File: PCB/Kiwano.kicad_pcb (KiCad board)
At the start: 2 copper layers, 63 x 63 mm, 50 parts, among them J1 VIK Module, J2 Cirque, J3 RGB_EX, SW1 PER56, U1 PMW3360DM-T2QU, U2 AP2127K-ADJ

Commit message: Fixed silk, moved production files.
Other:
- board text removed: "MISO Pullup"
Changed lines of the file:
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@@
     (property "ki_keywords" "R resistor")
     (attr smd)
-    (fp_text reference "R6" (at 0 1.5 180) (layer "B.SilkS")
+    (fp_text reference "R6" (at 0.3 1.5 180) (layer "B.SilkS")
         (effects (font (size 1 1) (thickness 0.15)) (justify mirror))
     )
@@
     (property "ki_keywords" "R resistor")
     (attr smd)
-    (fp_text reference "R9" (at 0 1.399998 -180) (layer "B.SilkS")
+    (fp_text reference "R9" (at -0.3 1.399998 -180) (layer "B.SilkS")
         (effects (font (size 1 1) (thickness 0.15)) (justify mirror))
     )
@@
     )
   )
-  (gr_line (start 84.7 46.3) (end 84.3 45.899999)
-    (stroke (width 0.12) (type default)) (layer "B.SilkS"))
-  (gr_line (start 81.6 47.1) (end 81.6 46.3)
-    (stroke (width 0.12) (type default)) (layer "B.SilkS"))
-  (gr_line (start 82 45.9) (end 84.3 45.899999)
+  (gr_line (start 84.8 35.35) (end 85 35.55)
     (stroke (width 0.12) (type default)) (layer "B.SilkS"))
   (gr_line (start 64.400013 52.729992) (end 63.700007 52.729992)
     (stroke (width 0.12) (type default)) (layer "B.SilkS"))
-  (gr_line (start 83.5 35.8) (end 83.5 37.1)
+  (gr_line (start 83.8 35.05) (end 83.8 36.35)
     (stroke (width 0.12) (type default)) (layer "B.SilkS"))
   (gr_line (start 83.1 54.8) (end 83.1 54)
     (stroke (width 0.12) (type default)) (layer "B.SilkS"))
-  (gr_line (start 81.6 46.3) (end 82 45.9)
+  (gr_line (start 81.8 35.3) (end 81.8 35)
+    (stroke (width 0.12) (type default)) (layer "B.SilkS"))
+  (gr_line (start 81.8 35.3) (end 81.6 35.5)
     (stroke (width 0.12) (type default)) (layer "B.SilkS"))
   (gr_line (start 63.700009 55.700002) (end 63.700007 57.179993)
@@
   (gr_line (start 63.700003 52.729994) (end 63.699998 54.2)
     (stroke (width 0.12) (type default)) (layer "B.SilkS"))
-  (gr_line (start 84.6 35) (end 85 35.4)
+  (gr_line (start 84.8 35.35) (end 84.8 35.05)
     (stroke (width 0.12) (type default)) (layer "B.SilkS"))
-  (gr_line (start 84.5 35.8) (end 84.5 37.1)
+  (gr_line (start 82.8 35.05) (end 82.8 36.35)
     (stroke (width 0.12) (type default)) (layer "B.SilkS"))
   (gr_circle (center 75 60) (end 76.149999 58.008146)
@@
     (effects (font (size 1 1) (thickness 0.15)) (justify mirror))
   )
-  (gr_text "MISO\nPullup" (at 84.7 47.6) (layer "B.SilkS")
-    (effects (font (size 1 1) (thickness 0.15)) (justify right mirror))
-  )
   (gr_text "+5V" (at 62.899998 51.2) (layer "B.SilkS")

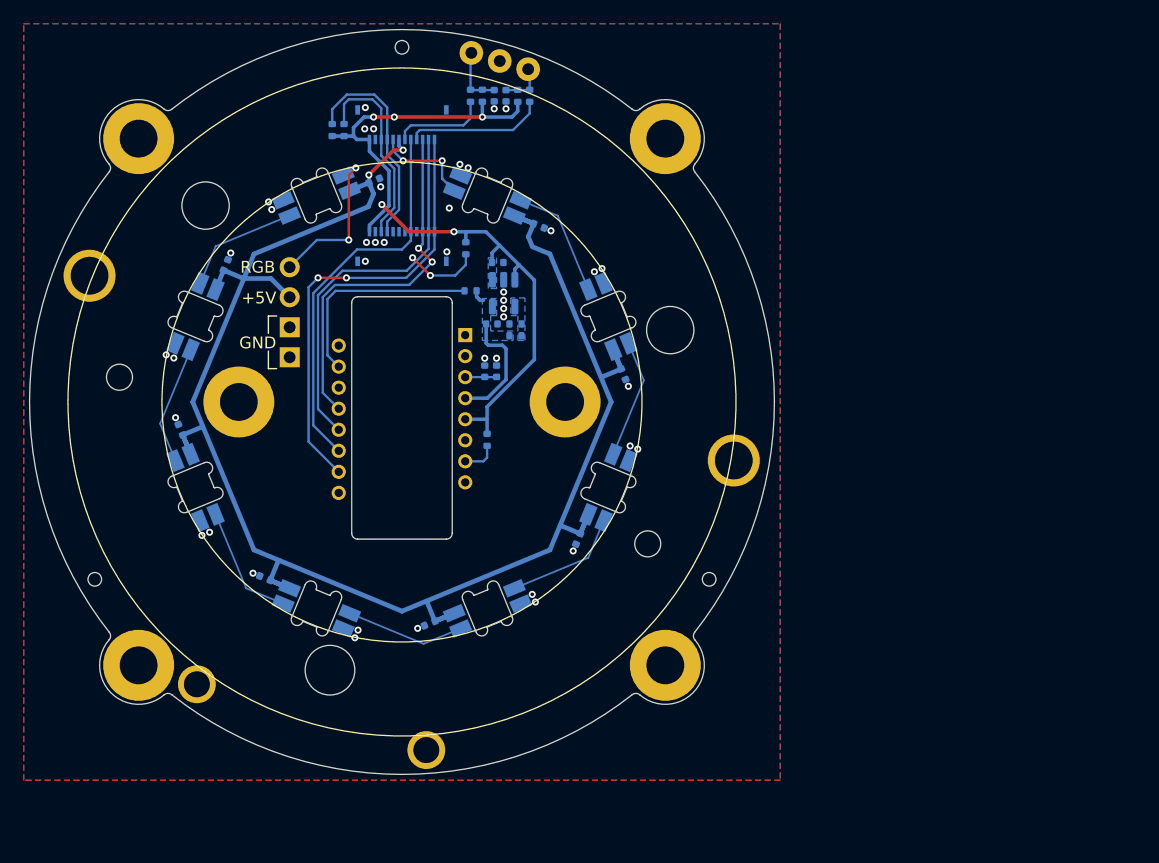
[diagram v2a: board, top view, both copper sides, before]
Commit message: 04/08/2023 update
Updated SK6812 MINI-E and switch footprints. Changed VIK FFC to FH12. Stitched ground planes together. Fixed VIK footprint. Moved production files to easier to access location.
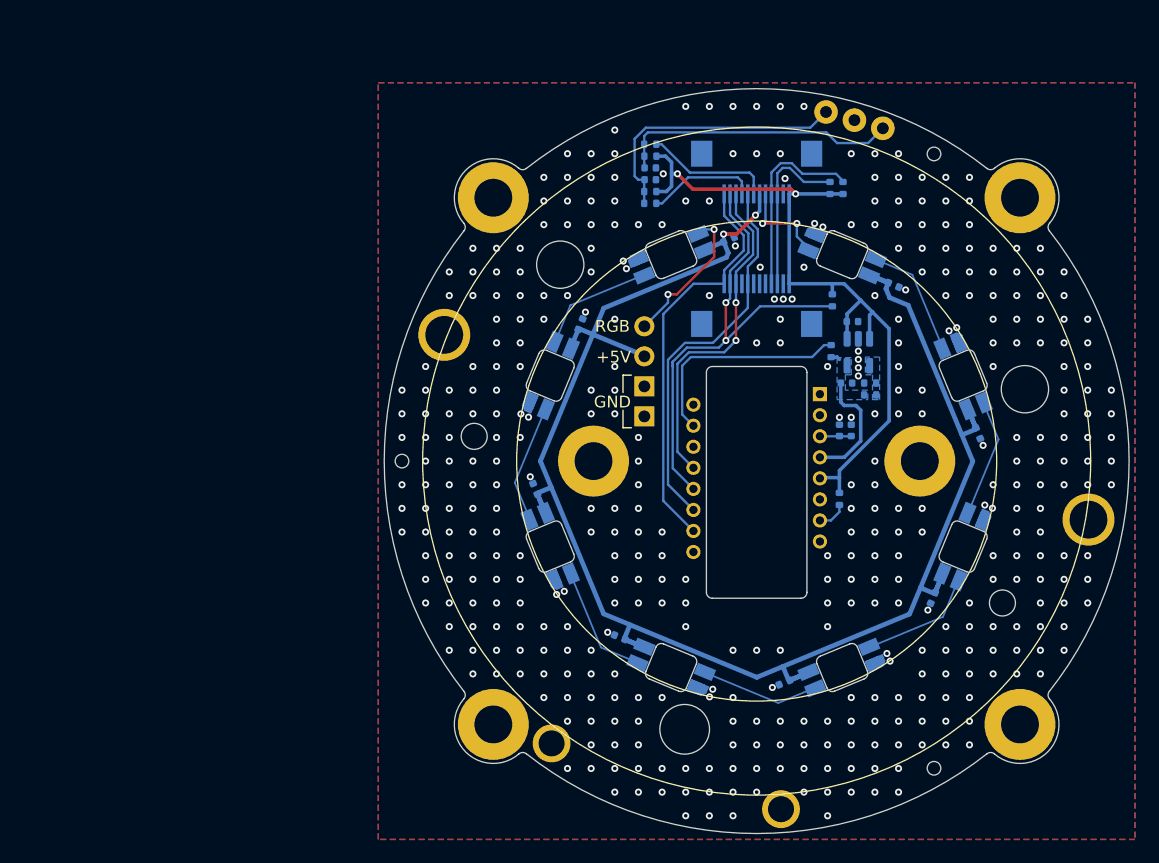
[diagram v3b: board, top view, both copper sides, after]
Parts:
- moved H3 72.8 mm to (120.0, 91.0), turned to -150 degrees
- moved R11 43.5 mm to (112.3, 41.9)
- moved R10 41.4 mm to (111.2, 41.9)
- moved H1 40.7 mm to (120.0, 39.0), turned to 132 degrees
- moved H2 35.0 mm to (75.0, 65.0), turned to -90 degrees
- moved R3 31.3 mm to (111.4, 51.4)
- moved R2 30.9 mm to (111.3, 55.7), turned to -90 degrees
- moved J1 30.4 mm to (105.0, 40.4)
- moved C3 30.4 mm to (119.9, 76.6)
- moved H6 30.4 mm to (82.7, 87.3)
- moved D1 30.4 mm to (112.2, 47.5)
- moved D6 30.4 mm to (87.5, 72.2)
- moved C12 30.4 mm to (112.6, 58.4)
- moved R5 30.4 mm to (114.6, 59.4)
- moved C11 30.4 mm to (113.1, 53.2)
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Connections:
- J1 pad 4: ROTA -> ROTB
- J1 pad 6: ROTB -> ROTA
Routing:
- net Net-(C13-Pad2): track 3.58 -> 23.9 mm
- net Net-(C14-Pad2): track 5.02 -> 23.3 mm
- net +3V3: track 66.2 -> 62.7 mm, vias 5 -> 2
- net SCK: track 38.0 -> 34.7 mm, vias 2 -> 0
- net CS: track 31.5 -> 28.7 mm
- net SDA: track 16.7 -> 14.5 mm
- net MISO: track 39.1 -> 41.1 mm
- net ROTA: track 11.8 -> 10.4 mm
- net ROTB: track 8.10 -> 8.95 mm
- net unconnected-(J2-DR-Pad9): track 0.00 -> 0.85 mm
- net Net-(U1-LED_P): track 18.0 -> 18.8 mm
- net SCL: track 18.2 -> 17.5 mm
- net Net-(D8-DOUT): track 12.7 -> 12.1 mm
- net GND: vias 41 -> 412
- removed copper zone on B.Cu, net +3V3
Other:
- outline, holes or cut-outs redrawn

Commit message: 28/08/2023 update
Unified component libraries into one big library. Fixed 3DP files.
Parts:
- A1: footprint Kiwano:Ariamelon_Logo_Mask -> Ariamelon-Logo:Ariamelon_Logo_Small_Mask
- A2: footprint Kiwano:vik-logo-small -> Ariamelon-Logo:VIK_Logo_Small
- D1, D2, D3, D4, D5, D6, D7, D8: footprint Kiwano:YS-SK6812MINI-E -> Ariamelon-Device:LED_OPSCO_SK6812MINI-E
- H1, H2, H3: footprint Kiwano:JLC Tooling Hole -> Ariamelon-HolePad:MountingHole_JLC-Tooling
- H4, H5, H6, H7, H8, H9: footprint Kiwano:MountingHole_3.2mm_M3_Pad -> Ariamelon-HolePad:MountingHole_3.2mm_M3_Pad
- J1: footprint Kiwano:vik-module-connector-horizontal -> Ariamelon-Connector:VIK_Module_Horizontal
- J2: value Cirque -> VIK Cirque Connector; footprint Kiwano:vik-cirque-connector-horizontal -> Ariamelon-Connector:VIK_Cirque_Horizontal
- J3: footprint Kiwano:Header_RGB -> Ariamelon-Header:PinHeader_RGB
- SW1: footprint Kiwano:PER56 -> Ariamelon-RotaryEncoder:RotaryEncoder_Bourns_PER561-P115-N0015
- U1: value PMW3360DM-T2QU -> PMW3360DM-T2QU_1; footprint Kiwano:IC_PMW3360DM-T2QU -> Ariamelon-Package:PixArt_PMW3360DM-T2QU

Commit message: V1.1 update
Changed LDO to XC6206P202MR. Removed RC filter and pullup from encoder pins.
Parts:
- removed C13, C14: 10n, Capacitor_SMD:C_0402_1005Metric
- removed R4, R6, R7, R8, R9: 10k, Resistor_SMD:R_0402_1005Metric
- removed R5: 15k, Resistor_SMD:R_0402_1005Metric
- U2: value AP2127K-ADJ -> XC6206P202MR; footprint Package_TO_SOT_SMD:SOT-23-5 -> Ariamelon-Package:SOT-23-3
- moved C12 0.60 mm to (113.2, 58.4)
- turned C11 to 0 degrees
- turned U2 to 90 degrees
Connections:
- SW1 pad A: Net-(C13-Pad2) -> ROTA
- SW1 pad B: Net-(C14-Pad2) -> ROTB
- U2 pad 1: +3V3 -> GND
- U2 pad 2: GND -> +2V
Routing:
- net Net-(C13-Pad2): track 23.9 -> 0.00 mm
- net Net-(C14-Pad2): track 23.3 -> 0.00 mm
- net +3V3: track 62.7 -> 43.1 mm, vias 2 -> 0
- net ROTA: track 10.4 -> 16.1 mm
- net ROTB: track 8.95 -> 11.8 mm
- net GND: vias 412 -> 424
- removed copper zone on B.Cu, net Net-(U2-ADJ)
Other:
- board text added: "Kiwano V1.1"
- board text removed: "Kiwano V1.0"
